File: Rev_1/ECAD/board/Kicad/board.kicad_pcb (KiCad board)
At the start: 2 copper layers, 110 parts, among them Q200 PMOS, Q201 PNP, Q202 PNP, SW300 6x6, SW301 6x6, SW302 6x6, SW303 6x6, U1 SD_CARD_READER, U100 ATMega328P-AU, U101 ICSP, U2 LCD OLED, U200 USB_C_6PIN, U202 FT232RL, U301 74HC245, U303 74HC245, U304 74HC595, U305 74HC595, U306 74HC595, U307 AT28C64B-15PU, U308 Summer, U4 L7805ABV, Y100 16MHZ

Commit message: Created a pcb file and added labels to footprints
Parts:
- moved U307 448.5 mm to (268.0, 76.2)
- moved C300 327.1 mm to (228.7, 129.9)
- moved C301 327.1 mm to (228.7, 132.9)
- moved C302 327.1 mm to (228.7, 136.0)
- moved C303 327.1 mm to (228.7, 139.0)
- moved C304 327.1 mm to (228.7, 142.0)
- moved C305 327.1 mm to (228.7, 145.0)
- moved D300 327.1 mm to (214.3, 109.3)
- moved D301 327.1 mm to (214.3, 112.3)
- moved D302 327.1 mm to (214.3, 115.4)
- moved D303 327.1 mm to (214.3, 118.4)
- moved D304 327.1 mm to (214.3, 121.5)
- moved D305 327.1 mm to (214.3, 124.5)
- moved D306 327.1 mm to (214.3, 127.5)
- moved D307 327.1 mm to (219.1, 109.3)
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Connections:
- U304 pad 12: /SHIFT_RCLK -> /SHIFT_SRCLK
- U305 pad 12: /SHIFT_RCLK -> /SHIFT_SRCLK
- U306 pad 12: /SHIFT_RCLK -> /SHIFT_SRCLK

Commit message: Made a ruf idea of the input protection on the pcb
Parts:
- added C306: 1u, Capacitor_SMD:C_0805_2012Metric_Pad1.18x1.45mm_HandSolder, F.Cu at (184.9, 115.4)
- added C307: 10n, Capacitor_SMD:C_0805_2012Metric_Pad1.18x1.45mm_HandSolder, F.Cu at (184.9, 118.4)
- added C308: 1u, Capacitor_SMD:C_0805_2012Metric_Pad1.18x1.45mm_HandSolder, F.Cu at (184.9, 121.5)
- added C309: 10n, Capacitor_SMD:C_0805_2012Metric_Pad1.18x1.45mm_HandSolder, F.Cu at (184.9, 124.5)
- added C310: 1u, Capacitor_SMD:C_0805_2012Metric_Pad1.18x1.45mm_HandSolder, F.Cu at (189.7, 115.4)
- added C311: 10n, Capacitor_SMD:C_0805_2012Metric_Pad1.18x1.45mm_HandSolder, F.Cu at (189.7, 118.4)
- added C312: 1u, Capacitor_SMD:C_0805_2012Metric_Pad1.18x1.45mm_HandSolder, F.Cu at (189.7, 121.5)
- added C313: 10n, Capacitor_SMD:C_0805_2012Metric_Pad1.18x1.45mm_HandSolder, F.Cu at (189.7, 124.5)
- added C314: 1u, Capacitor_SMD:C_0805_2012Metric_Pad1.18x1.45mm_HandSolder, F.Cu at (194.5, 115.4)
- added C315: 10n, Capacitor_SMD:C_0805_2012Metric_Pad1.18x1.45mm_HandSolder, F.Cu at (194.5, 118.4)
- added C316: 1u, Capacitor_SMD:C_0805_2012Metric_Pad1.18x1.45mm_HandSolder, F.Cu at (194.5, 121.5)
- added C317: 10n, Capacitor_SMD:C_0805_2012Metric_Pad1.18x1.45mm_HandSolder, F.Cu at (194.5, 124.5)
- moved C200 142.2 mm to (-84.5, 170.0), turned to 90 degrees
- moved Q200 140.7 mm to (-55.0, 166.0)
- moved Q201 138.8 mm to (-39.0, 169.0), turned to 180 degrees
- moved U201 138.7 mm to (-89.0, 170.0), turned to -90 degrees
- moved D200 136.2 mm to (-55.0, 171.0), turned to -90 degrees
- moved U203 135.0 mm to (-77.5, 169.0)
- moved R202 131.5 mm to (-55.0, 176.0), turned to -90 degrees
- moved D201 129.5 mm to (-48.0, 165.0), turned to 90 degrees
- moved R203 129.3 mm to (-52.0, 160.0)
- moved D202 129.2 mm to (-48.0, 176.0), turned to -90 degrees
- moved U200 128.9 mm to (-89.1, 155.0), turned to -90 degrees
- moved C201 128.5 mm to (-70.5, 170.0), turned to 90 degrees
- moved U202 125.4 mm to (-79.7, 181.0)
- moved R204 124.6 mm to (-48.0, 171.0), turned to -90 degrees
- moved Q202 124.5 mm to (-38.0, 163.0), turned to 180 degrees
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- renumbered U4 to U203, U303 to U302, U304 to U303, U305 to U304, U306 to U305, U307 to U306, U308 to U307
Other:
- copper layers 2 -> 4
- rule pad_to_mask_clearance: 0 -> 0.8
- board text added: "Power"
- board text added: "Reverse Polarity"

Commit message: Sorted most of the individual circuitri, time to start putting it all togheter
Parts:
- moved U301 152.9 mm to (356.7, 173.7)
- moved SW303 141.9 mm to (352.0, 149.0), turned to 180 degrees
- moved D320 141.2 mm to (364.0, 110.0), turned to -90 degrees
- moved SW302 138.5 mm to (351.0, 133.0), turned to 180 degrees
- moved D319 136.9 mm to (360.0, 110.0), turned to -90 degrees
- moved R306 134.2 mm to (361.0, 149.0)
- moved C303 133.1 mm to (361.0, 153.0)
- moved R304 132.9 mm to (361.0, 133.0)
- moved D318 132.6 mm to (356.0, 110.0), turned to -90 degrees
- moved R307 132.5 mm to (361.0, 145.0)
- moved R305 132.5 mm to (361.0, 129.0)
- moved C302 132.3 mm to (361.0, 137.0)
- moved D306 129.4 mm to (340.0, 97.0), turned to -90 degrees
- moved D317 128.4 mm to (352.0, 110.0), turned to -90 degrees
- moved D307 125.5 mm to (344.0, 97.0), turned to -90 degrees
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
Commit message: Layed out the input power circuit
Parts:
- moved U1 167.6 mm to (-38.0, 45.0)
- moved C201 155.9 mm to (34.0, 35.0), turned to 0 degrees
- moved C306 153.9 mm to (74.2, 222.4)
- moved C307 153.9 mm to (74.2, 225.4)
- moved C308 153.9 mm to (74.2, 228.4)
- moved C309 153.9 mm to (74.2, 231.4)
- moved R333 153.9 mm to (136.9, 230.9)
- moved R334 153.9 mm to (136.9, 233.9)
- moved U303 153.9 mm to (71.8, 249.0)
- moved U304 153.9 mm to (80.0, 249.0)
- moved C310 153.9 mm to (79.0, 222.4)
- moved C311 153.9 mm to (79.0, 225.4)
- moved C312 153.9 mm to (79.0, 228.4)
- moved C313 153.9 mm to (79.0, 231.4)
- moved C314 153.9 mm to (83.8, 222.4)
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
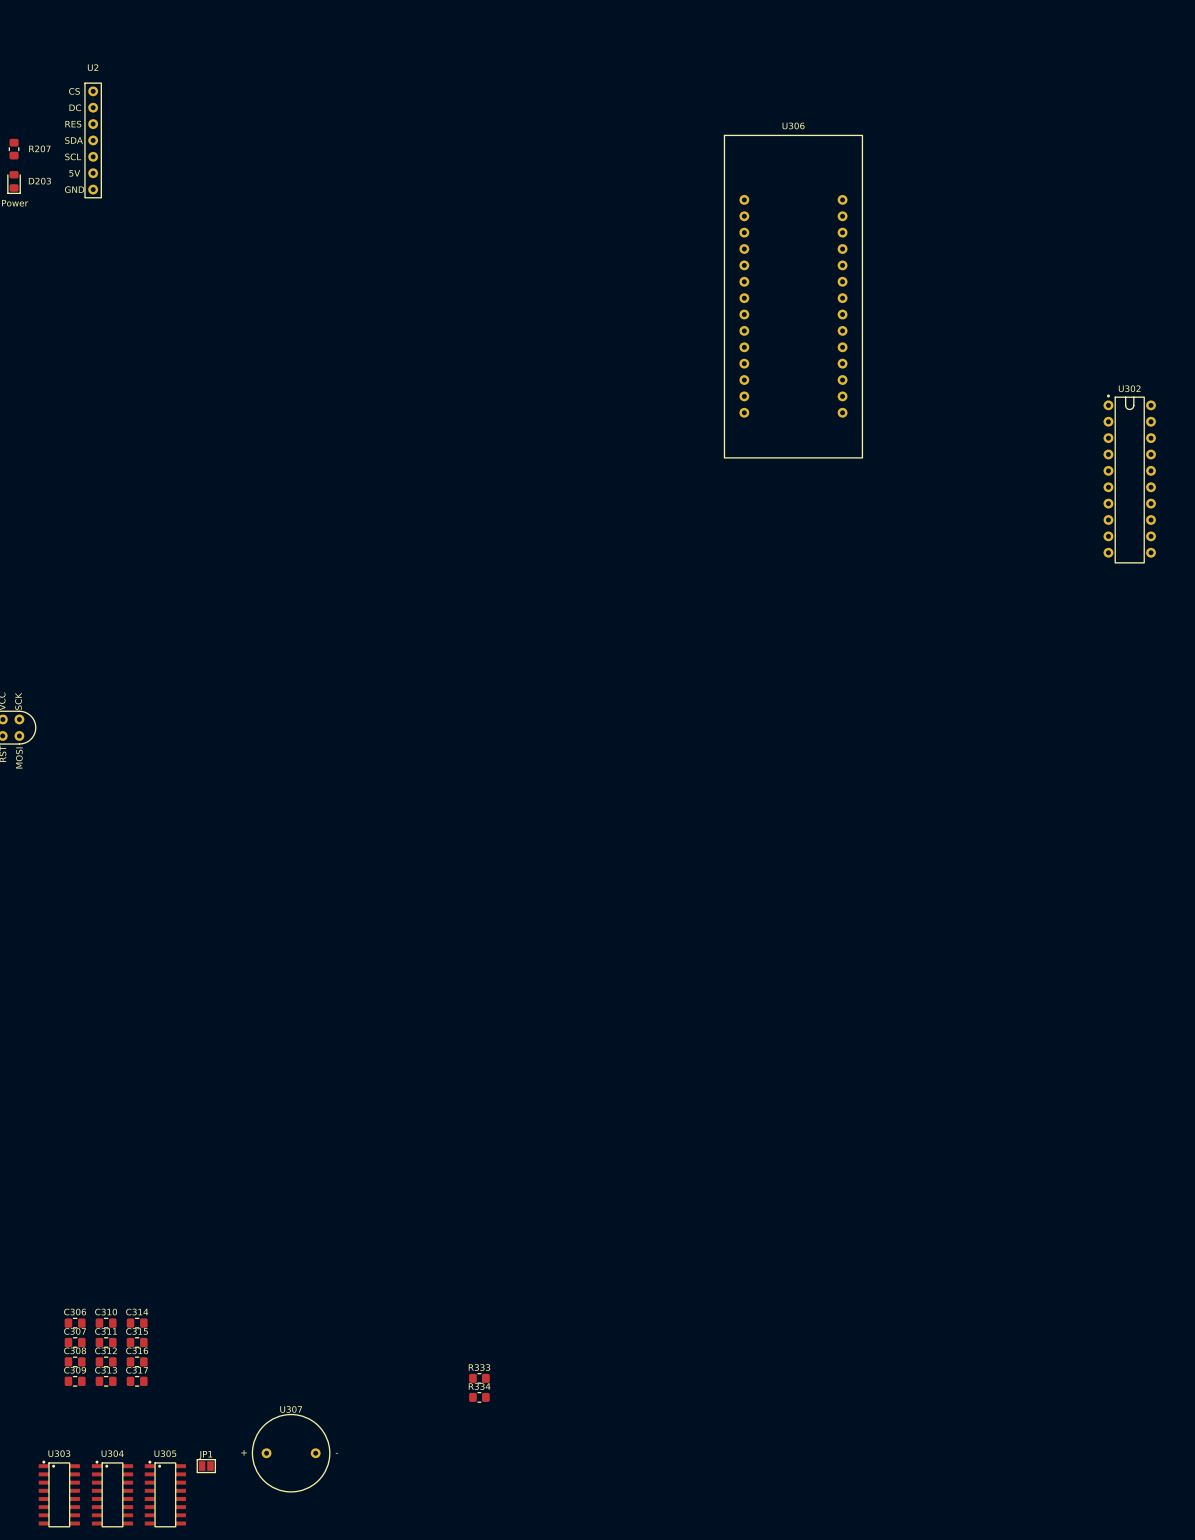
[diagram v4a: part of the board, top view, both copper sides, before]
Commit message: Made changes to the wiring in the shcematic to make it easier to route on the pcb, U305
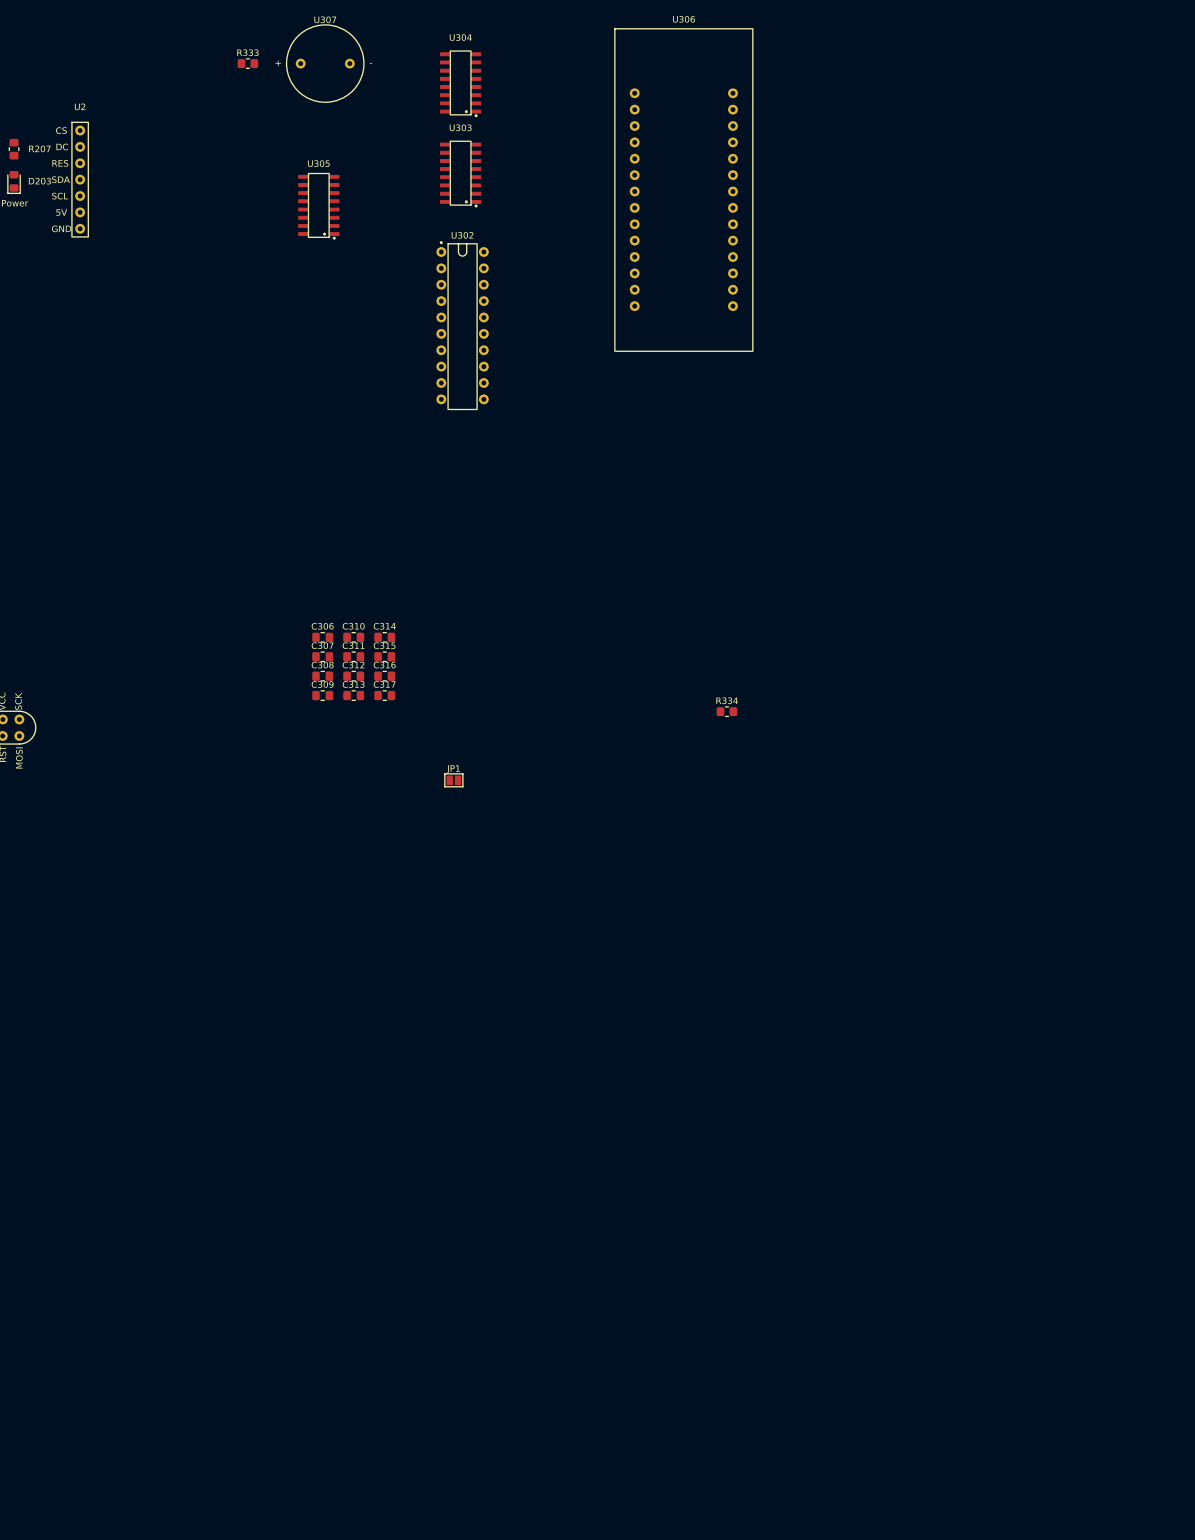
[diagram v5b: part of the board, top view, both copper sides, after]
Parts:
- moved U304 225.6 mm to (134.0, 30.0), turned to 180 degrees
- moved U307 215.6 mm to (113.0, 27.0)
- moved U303 214.2 mm to (134.0, 44.0), turned to 180 degrees
- moved R333 207.1 mm to (101.0, 27.0)
- moved U305 201.4 mm to (112.0, 49.0), turned to 180 degrees
- moved C306 113.1 mm to (112.6, 116.0)
- moved C307 113.1 mm to (112.6, 119.0)
- moved C310 113.1 mm to (117.4, 116.0)
- moved C311 113.1 mm to (117.4, 119.0)
- moved C314 113.1 mm to (122.2, 116.0)
- moved C315 113.1 mm to (122.2, 119.0)
- moved JP1 113.1 mm to (132.9, 138.2)
- moved C308 113.1 mm to (112.6, 122.0)
- moved C312 113.1 mm to (117.4, 122.0)
- moved C316 113.1 mm to (122.2, 122.0)
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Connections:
- net Net-(U303-QH') renamed /Data Logic/SER_CASCADE_1
- net Net-(U304-QH') renamed /Data Logic/SER_CASCADE_2
- U303 pad 11: Net-(U303-SRCLK) -> /SHIFT_SRCLK
- U303 pad 12: /SHIFT_SRCLK -> /SHIFT_RCLK
- U304 pad 11: Net-(U303-SRCLK) -> /SHIFT_SRCLK
- U304 pad 12: /SHIFT_SRCLK -> /SHIFT_RCLK
- U305 pad 1: /Data Logic/DATA_BUFFER_DIR -> /Data Logic/Summer_CL
- U305 pad 11: Net-(U303-SRCLK) -> /SHIFT_SRCLK
- U305 pad 12: /SHIFT_SRCLK -> /SHIFT_RCLK
- U305 pad 2: /Data Logic/DATA_BUFFER_OE -> /Data Logic/INPUT_BUFFER_OE
- U305 pad 3: /Data Logic/INPUT_BUFFER_OE -> /Data Logic/EEPROM_OE*
- U305 pad 4: /Data Logic/EEPROM_OE* -> /Data Logic/DATA_BUFFER_DIR
- U305 pad 5: /Data Logic/Summer_CL -> /Data Logic/DATA_BUFFER_OE

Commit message: Made some progress on the pcb
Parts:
- moved U301 314.1 mm to (50.8, 102.4), turned to -90 degrees
- moved R305 310.5 mm to (50.6, 121.9), turned to 90 degrees
- moved R304 306.6 mm to (54.6, 121.9), turned to 90 degrees
- moved R301 305.9 mm to (25.2, 121.9), turned to 90 degrees
- moved C302 302.8 mm to (58.6, 121.9), turned to 90 degrees
- moved R300 302.0 mm to (29.2, 121.9), turned to 90 degrees
- moved R307 298.6 mm to (63.3, 121.9), turned to 90 degrees
- moved C300 298.2 mm to (33.2, 121.9), turned to 90 degrees
- moved SW302 296.4 mm to (54.6, 132.1), turned to -90 degrees
- moved R306 294.9 mm to (67.3, 121.9), turned to 90 degrees
- moved R303 293.9 mm to (37.9, 121.9), turned to 90 degrees
- moved SW300 291.8 mm to (29.2, 132.1), turned to -90 degrees
- moved C303 291.4 mm to (71.3, 121.9), turned to 90 degrees
- moved R302 290.3 mm to (41.9, 121.9), turned to 90 degrees
- moved C301 286.7 mm to (45.9, 121.9), turned to 90 degrees
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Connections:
- C304 pad 2: /Data Logic/ROT_A -> /Data Logic/ROT_A_INPT
- C305 pad 2: /Data Logic/ROT_B -> /Data Logic/ROT_B_INPT
- R329 pad 2: /Data Logic/ROT_B -> /Data Logic/ROT_B_INPT
- R330 pad 2: /Data Logic/ROT_A -> /Data Logic/ROT_A_INPT
- U301 pad 13: /Data Logic/ROT_A -> /Data Logic/BUTTON_1
- U301 pad 14: /Data Logic/ROT_B -> /Data Logic/BUTTON_2
- U301 pad 15: /Data Logic/BUTTON_4 -> /Data Logic/BUTTON_3
- U301 pad 16: /Data Logic/BUTTON_3 -> /Data Logic/BUTTON_4
- U301 pad 17: /Data Logic/BUTTON_2 -> /Data Logic/ROT_A_INPT
- U301 pad 18: /Data Logic/BUTTON_1 -> /Data Logic/ROT_B_INPT

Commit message: Most of the things are put to its place, LED indicators still needs some configuration, and som testpoints should be added!
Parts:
- moved D308 204.3 mm to (111.8, 113.4)
- moved D309 204.3 mm to (115.8, 113.4)
- moved D310 204.3 mm to (119.8, 113.4)
- moved D311 204.3 mm to (123.8, 113.4)
- moved D312 204.3 mm to (127.8, 113.4)
- moved D313 204.3 mm to (131.8, 113.4)
- moved D314 204.3 mm to (135.8, 113.4)
- moved D315 204.3 mm to (139.8, 113.4)
- moved D316 204.3 mm to (143.8, 113.4)
- moved D317 204.3 mm to (147.8, 113.3)
- moved D318 204.3 mm to (151.8, 113.3)
- moved D319 204.3 mm to (155.8, 113.4)
- moved D320 204.3 mm to (159.7, 113.4)
- moved R316 204.3 mm to (111.8, 119.4)
- moved R317 204.3 mm to (115.8, 119.4)
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
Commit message: Everything finished, can start routing
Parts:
- C200: value u33 -> 330n
- C201: value u1 -> 100n
- D201, D202: footprint Diode_SMD:D_0805_2012Metric_Pad1.15x1.40mm_HandSolder -> Diode_THT:D_DO-35_SOD27_P3.81mm_Vertical_KathodeUp
- Q200: footprint Package_TO_SOT_THT:TO-92 -> Package_TO_SOT_SMD:SOT-23
- moved C317 129.4 mm to (173.0, 31.0), turned to -90 degrees
- moved C316 128.4 mm to (177.0, 31.0), turned to -90 degrees
- moved C315 94.4 mm to (95.0, 50.8), turned to 90 degrees
- moved C314 92.4 mm to (91.0, 51.0), turned to 90 degrees
- moved U306 28.4 mm to (159.6, 75.0)
- moved C308 6.43 mm to (136.0, 62.0)
- moved C309 6.43 mm to (132.0, 62.0)
- moved U302 2.65 mm to (125.2, 74.9)
